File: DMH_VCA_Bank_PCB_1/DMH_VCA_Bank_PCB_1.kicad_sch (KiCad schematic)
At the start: 0 parts

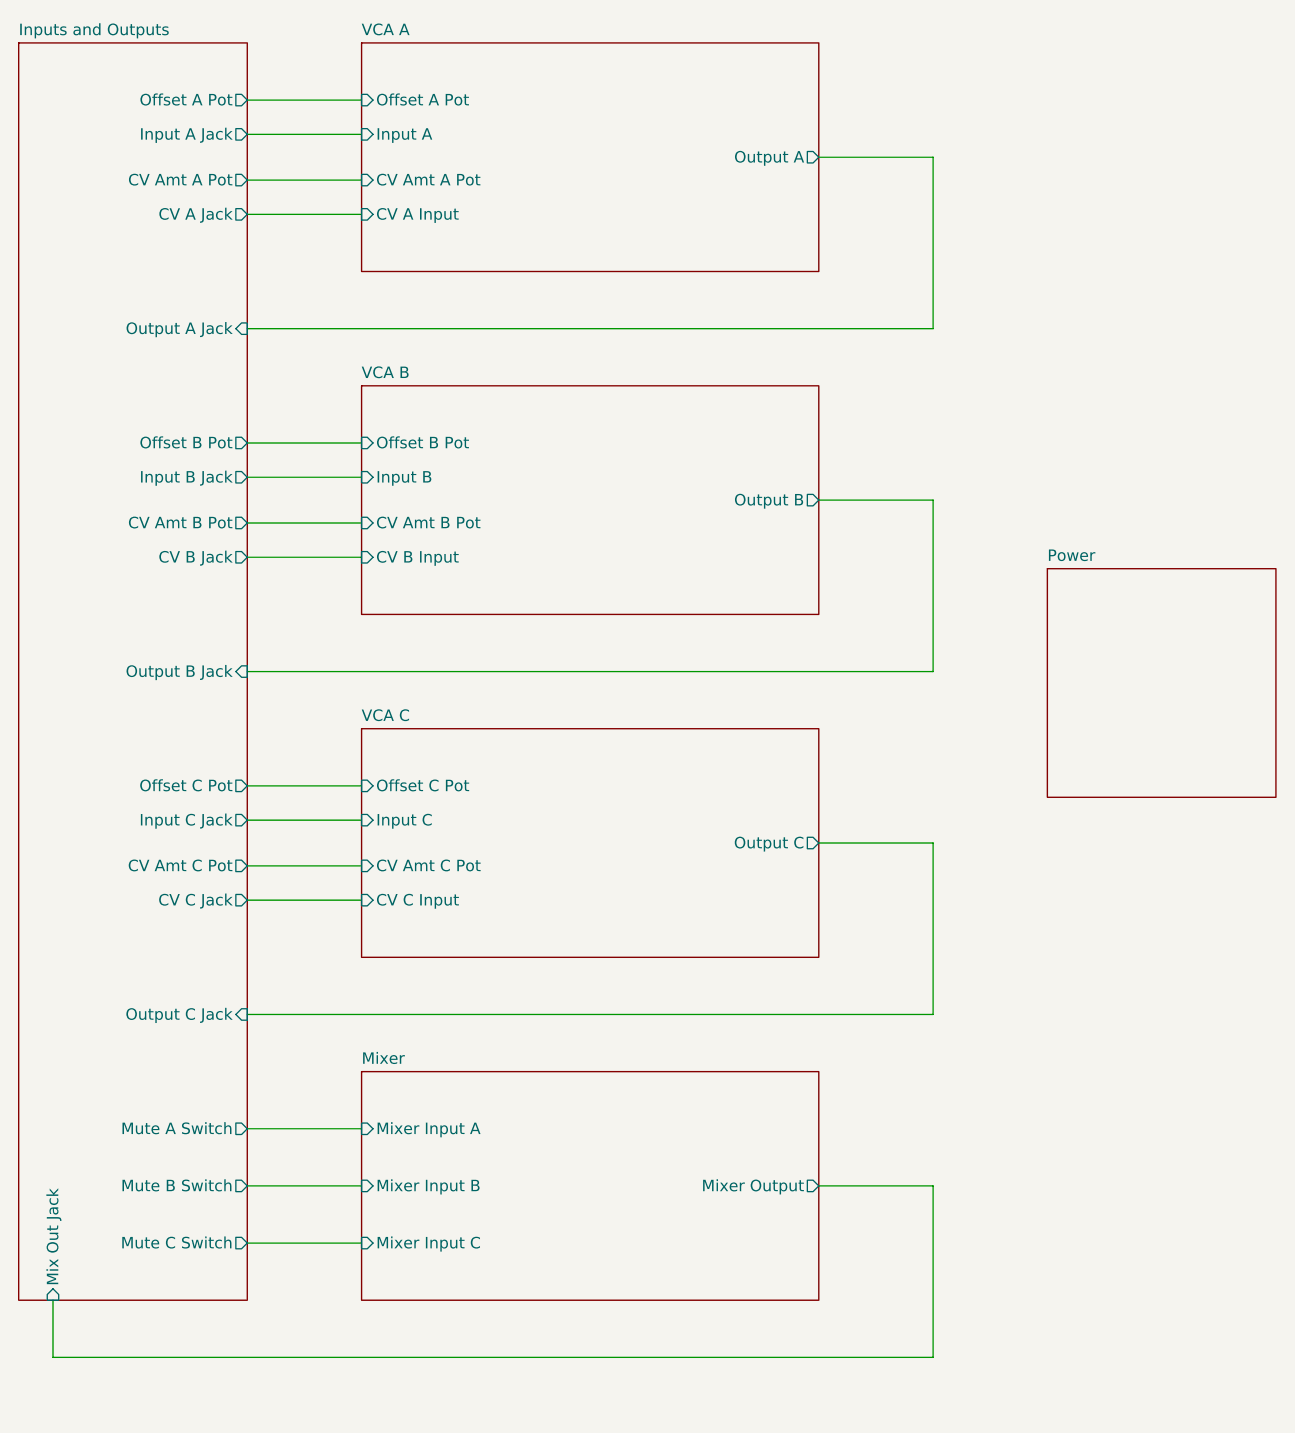
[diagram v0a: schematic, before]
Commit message: Finished schematic of PCB 1
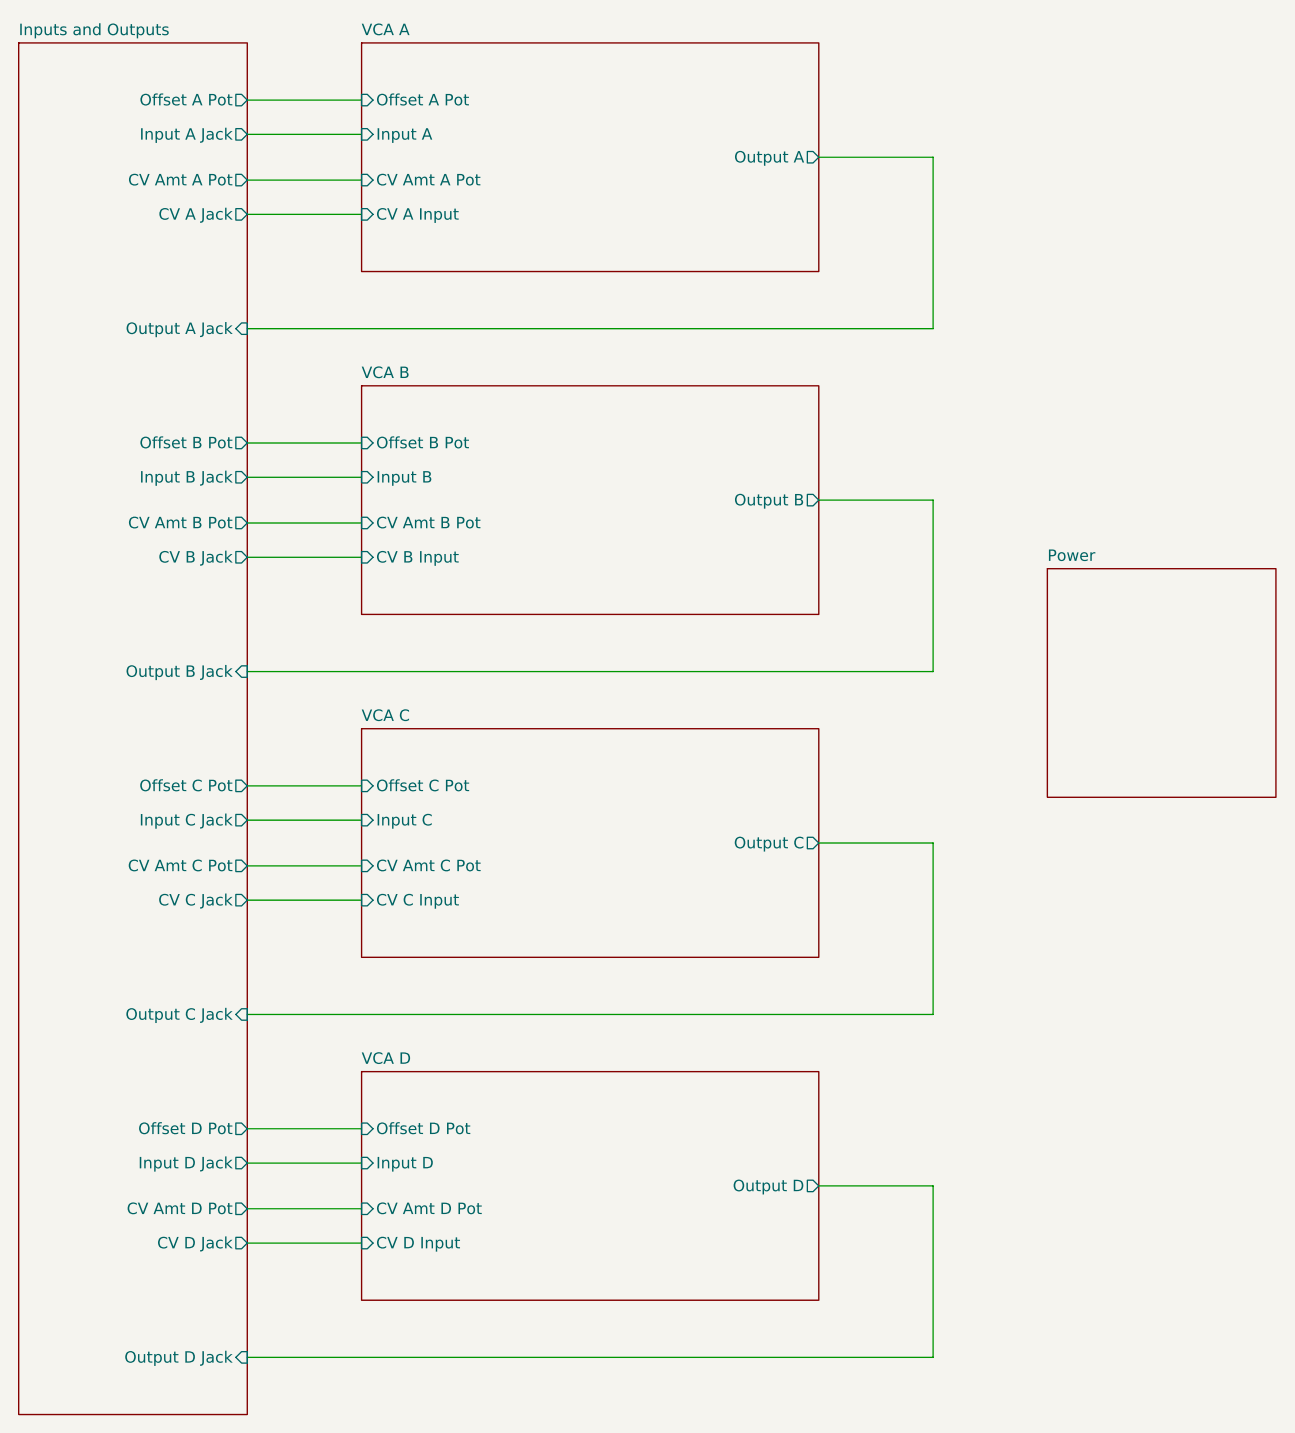
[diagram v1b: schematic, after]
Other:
- removed sheet Mixer
- added sheet VCA D (VCA_D.kicad_sch)
- sheet Inputs and Outputs ports: added CV Amt D Pot, CV D Jack, Input D Jack, Offset D Pot, Output D Jack; removed Mix Out Jack, Mute A Switch, Mute B Switch, Mute C Switch
